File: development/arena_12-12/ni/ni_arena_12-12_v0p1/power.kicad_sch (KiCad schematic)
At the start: 2 parts, among them J1 Barrel_Jack, SW1 SW_SPDT

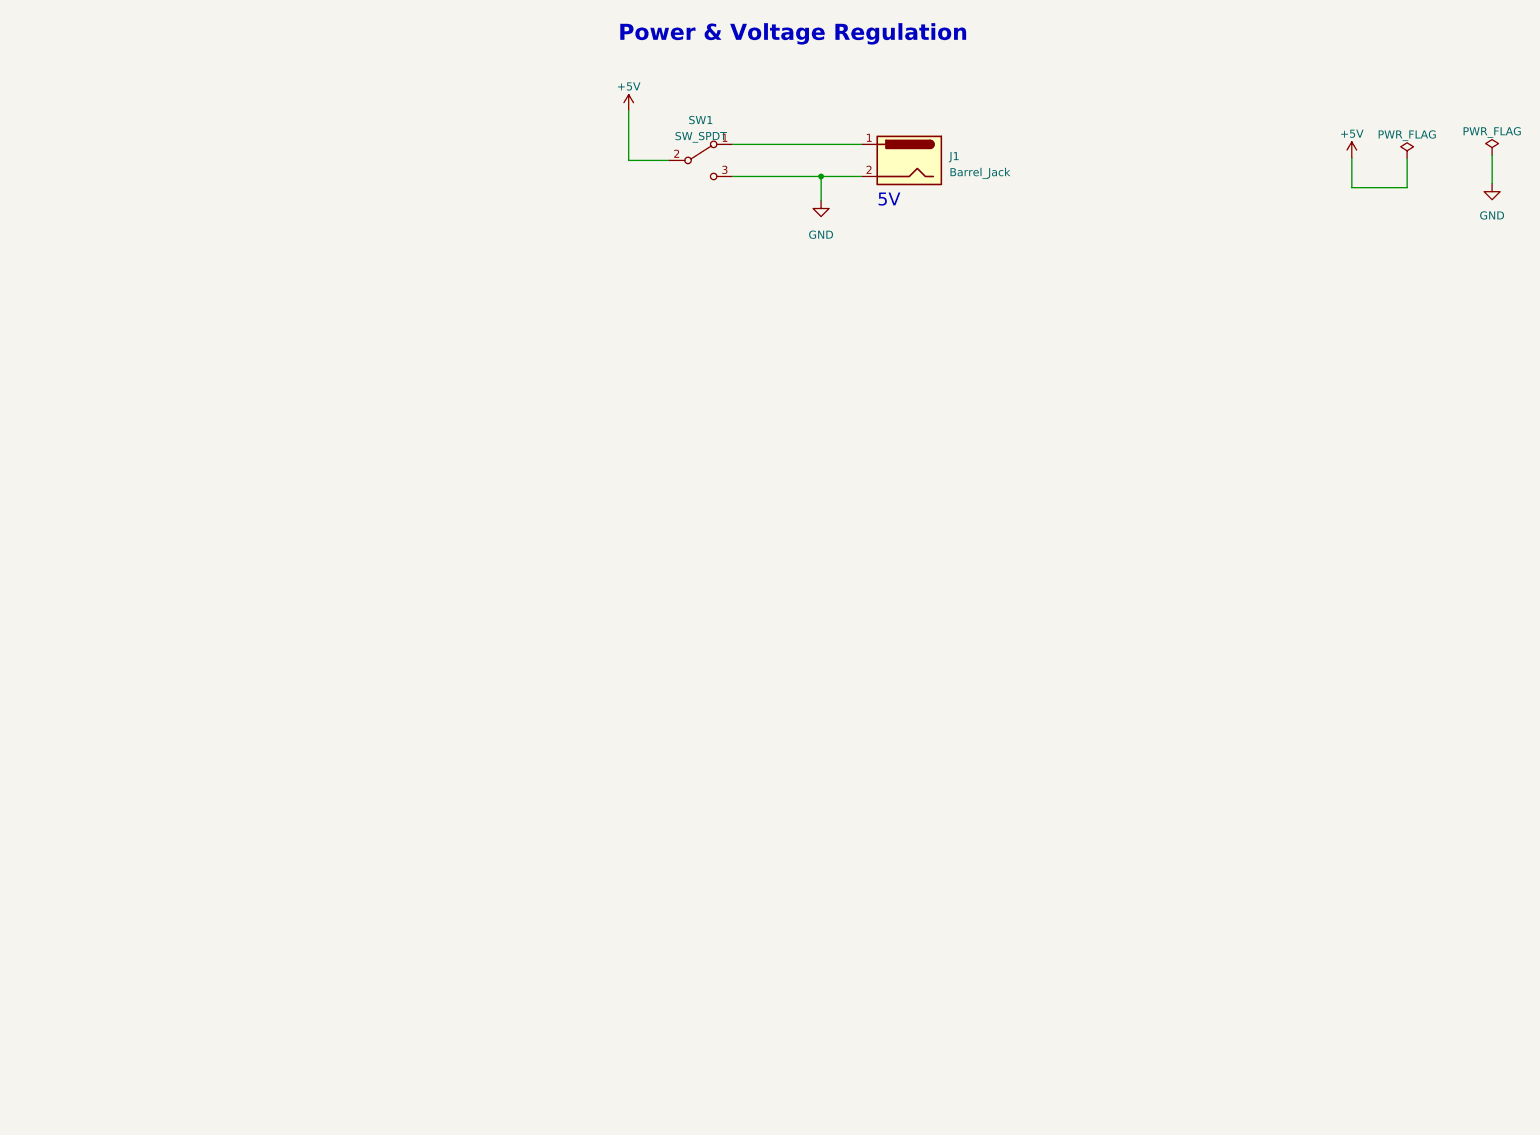
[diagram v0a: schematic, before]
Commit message: Finished initial schematic and layout for 12-12 NI arena (without voltage regulators).
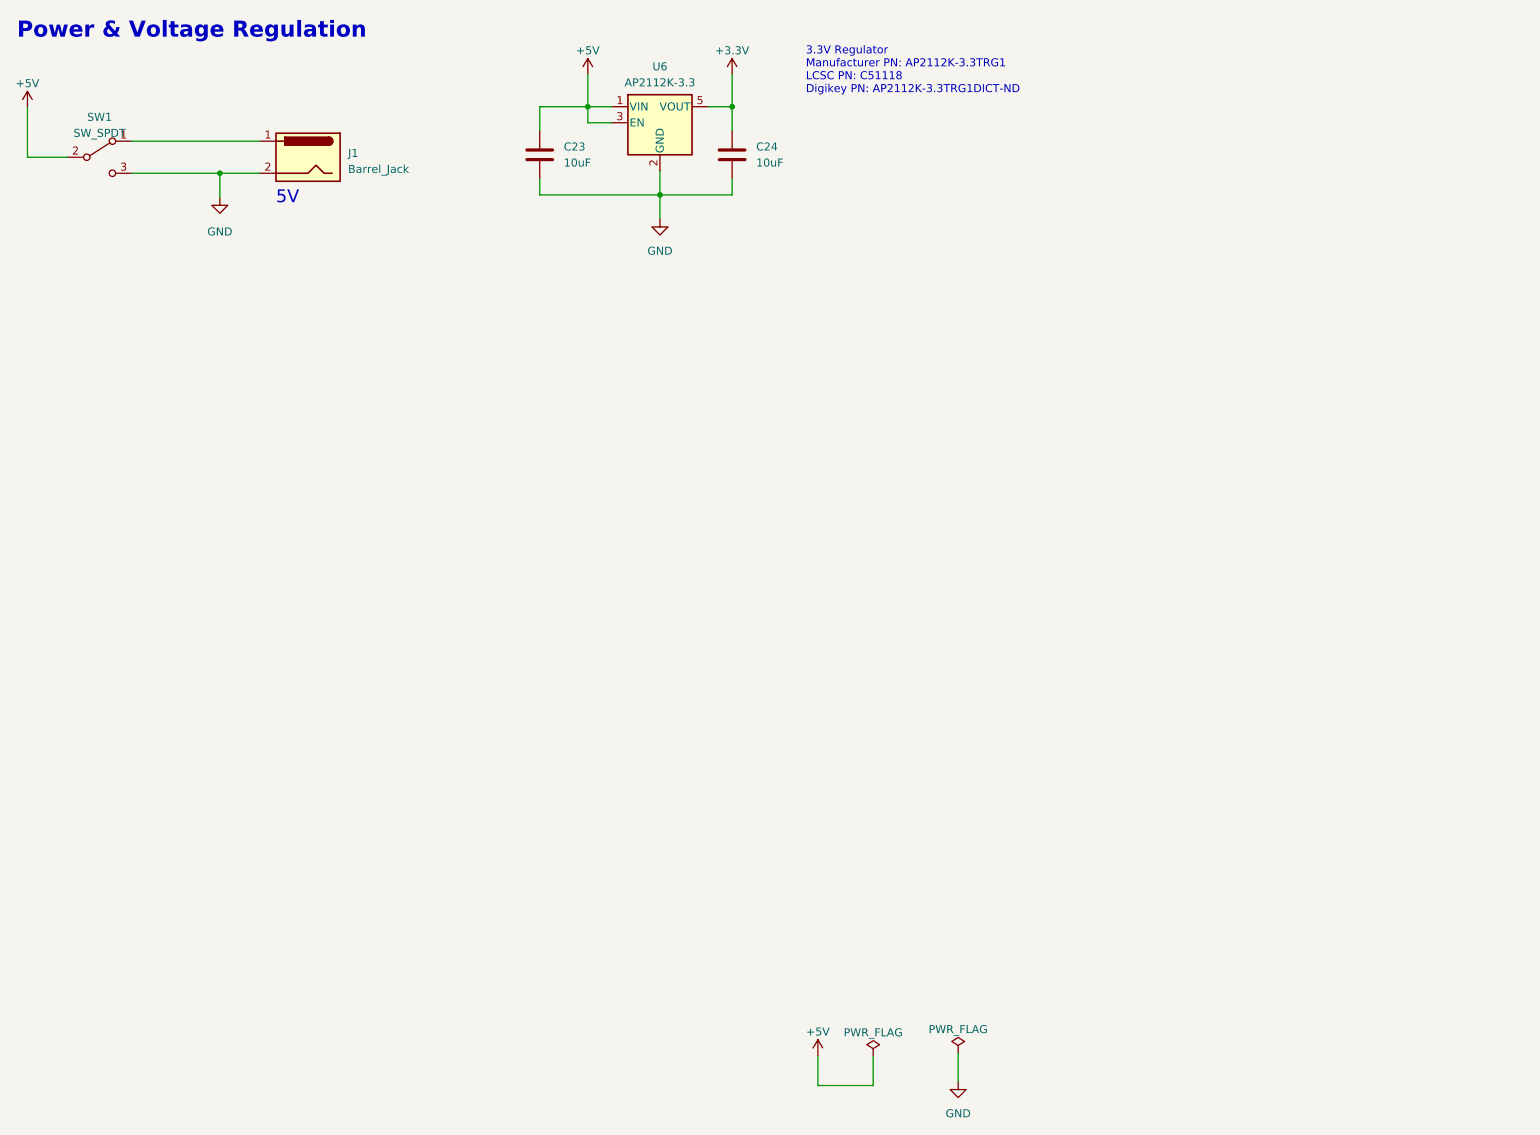
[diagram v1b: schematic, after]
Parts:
- added C23, C24: 10uF, Capacitor_SMD:C_0603_1608Metric, symbol Device:C
- added U6: AP2112K-3.3, Package_TO_SOT_SMD:SOT-23-5, symbol Regulator_Linear:AP2112K-3.3
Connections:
- net +5V: now also C23.1, U6.1 (VIN), U6.3 (EN)
- net GND: now also C23.2, C24.2, U6.2 (GND)
- new net +3.3V: C24.1, U6.5 (VOUT)
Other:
- note added: "3.3V Regulator Manufacturer PN: AP2112K-3.3TRG1 LCSC PN: C51118 Digikey PN: AP2112K-3.3TRG1DICT-ND"
- moved on the sheet: J1, SW1
